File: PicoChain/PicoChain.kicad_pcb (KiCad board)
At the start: 2 copper layers, 14 parts, among them J1 RJ45, J2 RJ45, J3 Conn_01x02_Socket, J4 Conn_01x02_Socket, J5 Conn_01x20_Socket, J6 Conn_01x20_Socket, U1 PCA9615DP, U2 RASPBERRY_PI_PICO

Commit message: Updated to version 1.1
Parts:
- removed J3, J4: Conn_01x02_Socket, Connector_PinHeader_2.54mm:PinHeader_1x02_P2.54mm_Vertical
- removed R1, R3, R4, R6: 470, Resistor_SMD:R_0805_2012Metric
- removed R2, R5: 140, Resistor_SMD:R_0805_2012Metric
- added +12V: GND, Connector_PinHeader_2.54mm:PinHeader_1x02_P2.54mm_Vertical, F.Cu at (128.5, 112.6)
- added +5V: GND, Connector_PinHeader_2.54mm:PinHeader_1x02_P2.54mm_Vertical, F.Cu at (128.5, 96.1)
- added C1: 330nF, Capacitor_Tantalum_SMD:CP_EIA-3216-18_Kemet-A, F.Cu at (150.4, 82.6)
- added C2: 330nF, Capacitor_Tantalum_SMD:CP_EIA-3216-18_Kemet-A, F.Cu at (165.6, 82.9)
- added C3: 330nF, Capacitor_Tantalum_SMD:CP_EIA-3216-18_Kemet-A, F.Cu at (162.1, 82.9)
- added C4: 330nF, Capacitor_Tantalum_SMD:CP_EIA-3216-18_Kemet-A, F.Cu at (153.9, 82.6)
- added C5: 10uF, Capacitor_Tantalum_SMD:CP_EIA-3528-21_Kemet-B, F.Cu at (158.8, 108.8)
- added C6: 10uF, Capacitor_Tantalum_SMD:CP_EIA-3528-21_Kemet-B, F.Cu at (158.8, 104.0)
- added U3: LM78M05, Package_TO_SOT_SMD:TO-252-2, F.Cu at (163.3, 73.8)
- added U4: LM78M05, Package_TO_SOT_SMD:TO-252-2, F.Cu at (152.7, 73.7)
- added U5: LM1085-12, LM1085IS-12:TO254P1524X483-4N, F.Cu at (170.2, 105.0)
- U2: footprint MCU_RaspberryPi_and_Boards:RPi_Pico_SMD_TH -> RASPBERRY_PI_PICO:RASPBERRY_PI_PICO
- moved J6 93.2 mm to (182.0, 119.6), turned to -90 degrees
- moved J5 45.2 mm to (133.7, 91.7), turned to 90 degrees
- moved U2 38.1 mm to (159.1, 105.7), turned to -90 degrees
- moved J1 34.2 mm to (143.7, 83.4), turned to 180 degrees
- moved J2 29.5 mm to (181.8, 83.4), turned to 180 degrees
- moved U1 20.9 mm to (158.3, 85.2), turned to 90 degrees
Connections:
- J1 pad 1: Net-(U1-DSCLM) -> GND
- J1 pad 2: Net-(U1-DSCLP) -> +24V
- J1 pad 3: +5V -> Net-(U1-DSCLM)
- J1 pad 4: GND -> Net-(U1-DSCLP)
- J1 pad 5: /+5V(M) -> Net-(U1-DSDAP)
- J1 pad 6: +12V -> Net-(U1-DSDAM)
- J1 pad 7: Net-(U1-DSDAM) -> GND
- J1 pad 8: Net-(U1-DSDAP) -> +12V
- J2 pad 1: Net-(U1-DSCLM) -> GND
- J2 pad 2: Net-(U1-DSCLP) -> +24V
- J2 pad 3: +5V -> Net-(U1-DSCLM)
- J2 pad 4: GND -> Net-(U1-DSCLP)
- J2 pad 5: /+5V(M) -> Net-(U1-DSDAP)
- J2 pad 6: +12V -> Net-(U1-DSDAM)
- J2 pad 7: Net-(U1-DSDAM) -> GND
- J2 pad 8: Net-(U1-DSDAP) -> +12V
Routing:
- net +24V: track 0.00 -> 86.2 mm, vias 0 -> 1
- net +5V: track 0.00 -> 84.0 mm
- net +12V: track 0.00 -> 83.4 mm, vias 0 -> 1
- net Net-(U1-DSCLP): track 0.00 -> 50.7 mm, vias 0 -> 2
- net Net-(U1-DSDAM): track 0.00 -> 49.9 mm, vias 0 -> 2
- net /+5V(M): track 0.00 -> 45.6 mm, vias 0 -> 1
- net Net-(U1-DSDAP): track 0.00 -> 43.9 mm, vias 0 -> 2
- net Net-(U1-DSCLM): track 0.00 -> 43.2 mm, vias 0 -> 2
- net /+12V(R): track 0.00 -> 39.3 mm
- net Net-(J5-Pin_15): track 0.00 -> 27.9 mm, vias 0 -> 1
- net Net-(J5-Pin_14): track 0.00 -> 26.3 mm, vias 0 -> 1
- net Net-(J6-Pin_9): track 0.00 -> 5.08 mm
- net Net-(J6-Pin_8): track 0.00 -> 5.08 mm
- net Net-(J6-Pin_7): track 0.00 -> 5.08 mm
- net Net-(J6-Pin_6): track 0.00 -> 5.08 mm
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- added copper zone on B.Cu, net GND
- added copper zone on F.Cu, net GND
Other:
- board outline added: 60 x 54 mm
- board text added: "Jason Alexander"
- board text added: "PicoDaisy"
- board text added: "PicoDaisy (v1.1)"

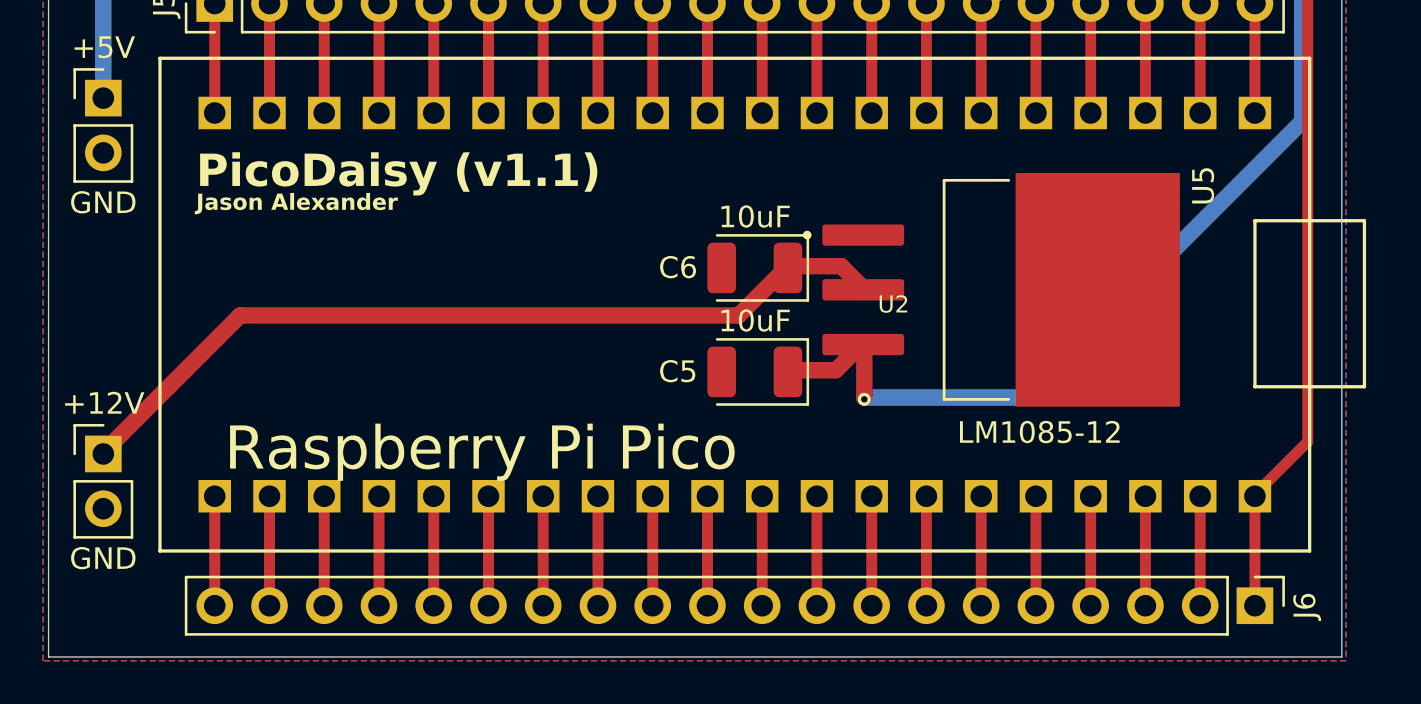
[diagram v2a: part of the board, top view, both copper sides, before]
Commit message: Added open source hardware logo to PCBs
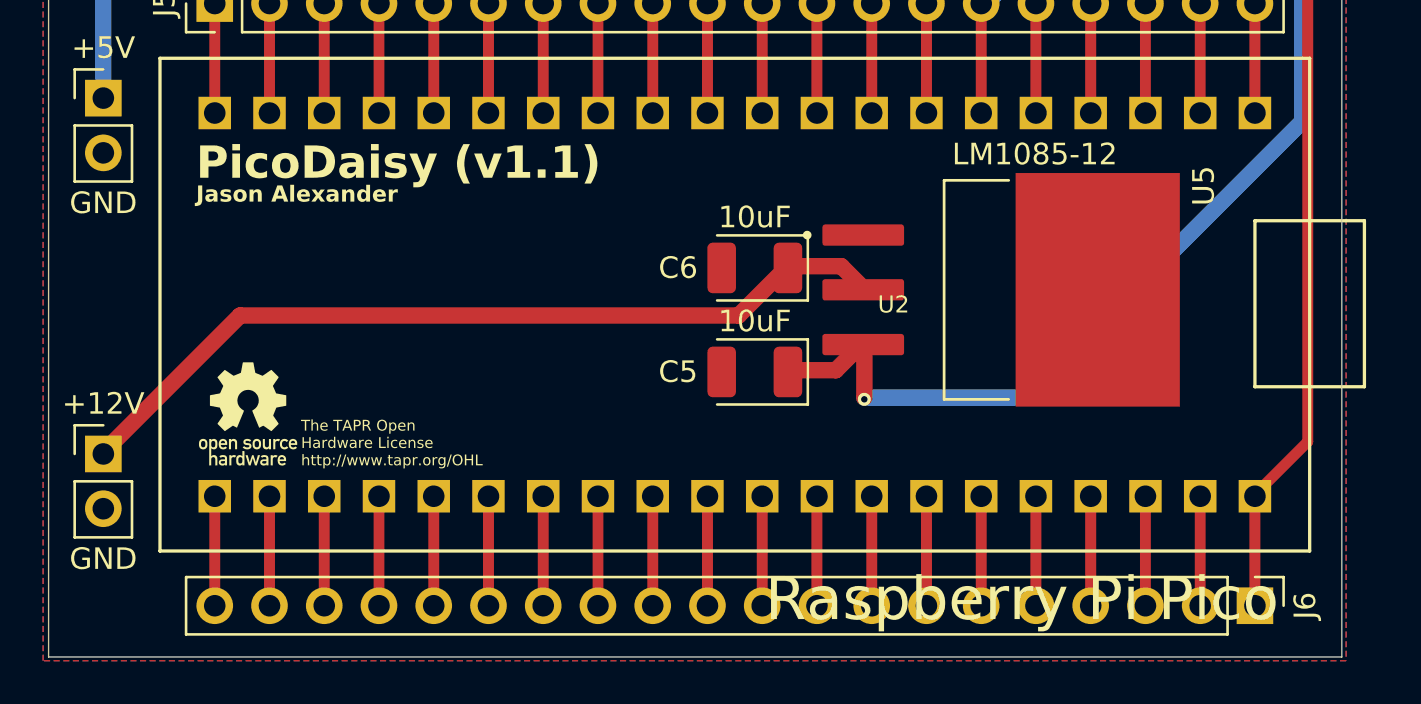
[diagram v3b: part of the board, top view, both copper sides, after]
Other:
- board text added: "The TAPR Open Hardware License http://www.tapr.org/OHL"

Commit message: Regenerated gerbers
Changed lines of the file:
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@@
 		)
 		(fp_text user "Raspberry Pi Pico"
-			(at 13.663056 -12.054914 0)
+			(at 0.0114 15.5994 0)
 			(layer "F.SilkS")
 			(effects
 				(font
-					(size 2 2)
+					(size 1.75 1.75)
 					(thickness 0.15)
 				)

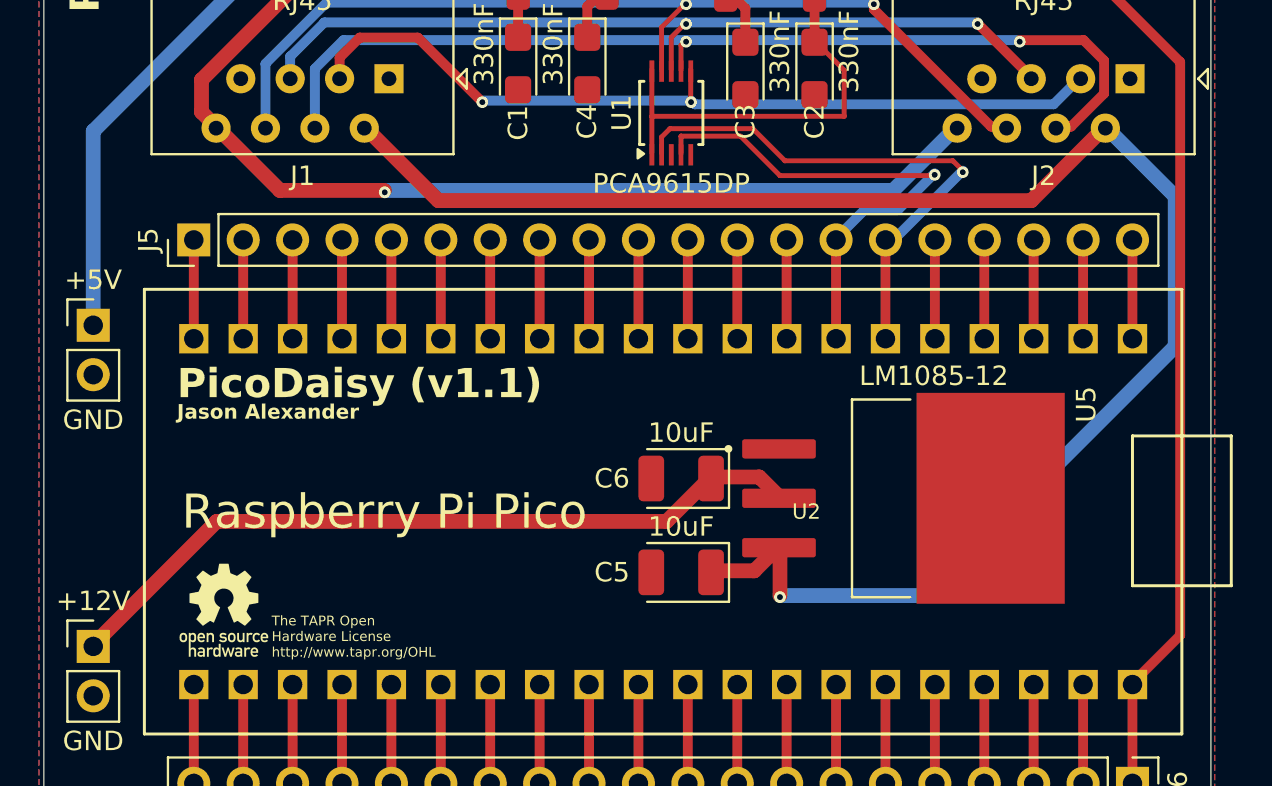
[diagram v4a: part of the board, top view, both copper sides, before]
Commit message: Made pass through power rails larger.
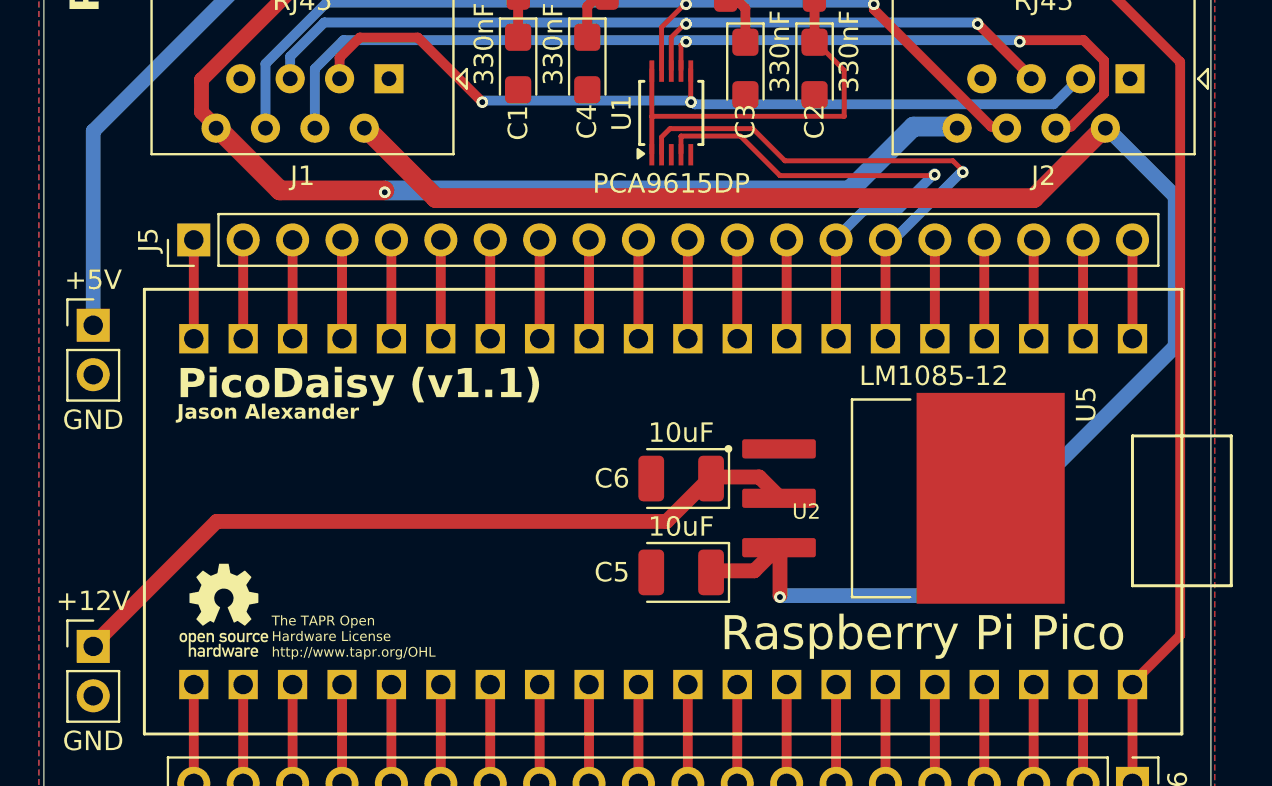
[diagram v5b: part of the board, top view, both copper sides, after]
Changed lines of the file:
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@@
 		)
 		(fp_text user "Raspberry Pi Pico"
-			(at 0.0114 15.5994 0)
+			(at 6.2598 -12.0866 0)
 			(layer "F.SilkS")
 			(effects
@@
 		(start 138.1365 89.138)
 		(end 143.51 89.138)
-		(width 0.762)
+		(width 1.016)
 		(layer "F.Cu")
 		(net 5)
@@
 		(start 134.8545 85.856)
 		(end 138.1365 89.138)
-		(width 0.762)
+		(width 1.016)
 		(layer "F.Cu")
 		(net 5)
@@
 	)
 	(segment
+		(start 167.4274 89.138)
+		(end 170.7094 85.856)
+		(width 1.016)
+		(layer "B.Cu")
+		(net 5)
+	)
+	(segment
 		(start 143.51 89.138)
 		(end 143.526 89.154)
@@
 	)
 	(segment
-		(start 169.6725 89.138)
-		(end 172.9545 85.856)
+		(start 143.526 89.154)
+		(end 143.542 89.138)
 		(width 0.762)
 		(layer "B.Cu")
@@
 	)
 	(segment
-		(start 143.542 89.138)
-		(end 169.6725 89.138)
-		(width 0.762)
+		(start 170.7094 85.856)
+		(end 172.9545 85.856)
+		(width 1.016)
 		(layer "B.Cu")
 		(net 5)
 	)
 	(segment
-		(start 143.526 89.154)
-		(end 143.542 89.138)
-		(width 0.762)
+		(start 143.542 89.138)
+		(end 167.4274 89.138)
+		(width 1.016)
 		(layer "B.Cu")
 		(net 5)
@@
 	)
 	(segment
-		(start 176.7685 89.662)
+		(start 176.8955 89.535)
 		(end 180.5745 85.856)
-		(width 0.762)
+		(width 1.016)
 		(layer "F.Cu")
 		(net 48)
 	)
 	(segment
-		(start 142.4745 85.856)
-		(end 146.2805 89.662)
+		(start 163.846 107.476)
+		(end 163.796 107.426)
 		(width 0.762)
 		(layer "F.Cu")
@@
 	)
 	(segment
-		(start 163.846 107.476)
+		(start 162.526 108.696)
 		(end 163.796 107.426)
 		(width 0.762)
@@
 	)
 	(segment
-		(start 146.2805 89.662)
-		(end 176.7685 89.662)
-		(width 0.762)
+		(start 146.1535 89.535)
+		(end 176.8955 89.535)
+		(width 1.016)
 		(layer "F.Cu")
 		(net 48)
 	)
 	(segment
-		(start 162.526 108.696)
-		(end 163.796 107.426)
-		(width 0.762)
+		(start 142.4745 85.856)
+		(end 146.1535 89.535)
+		(width 1.016)
 		(layer "F.Cu")
 		(net 48)

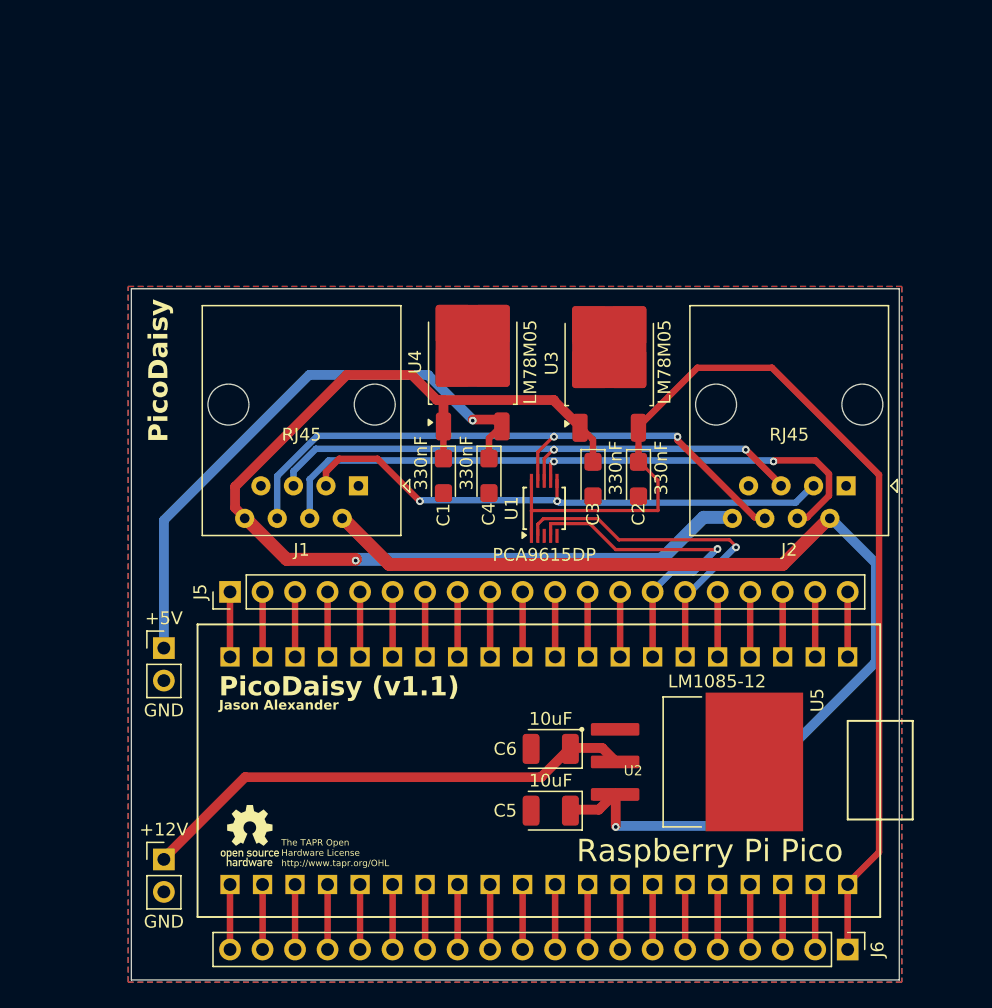
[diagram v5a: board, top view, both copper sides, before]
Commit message: Updated PicoChainZero base board.
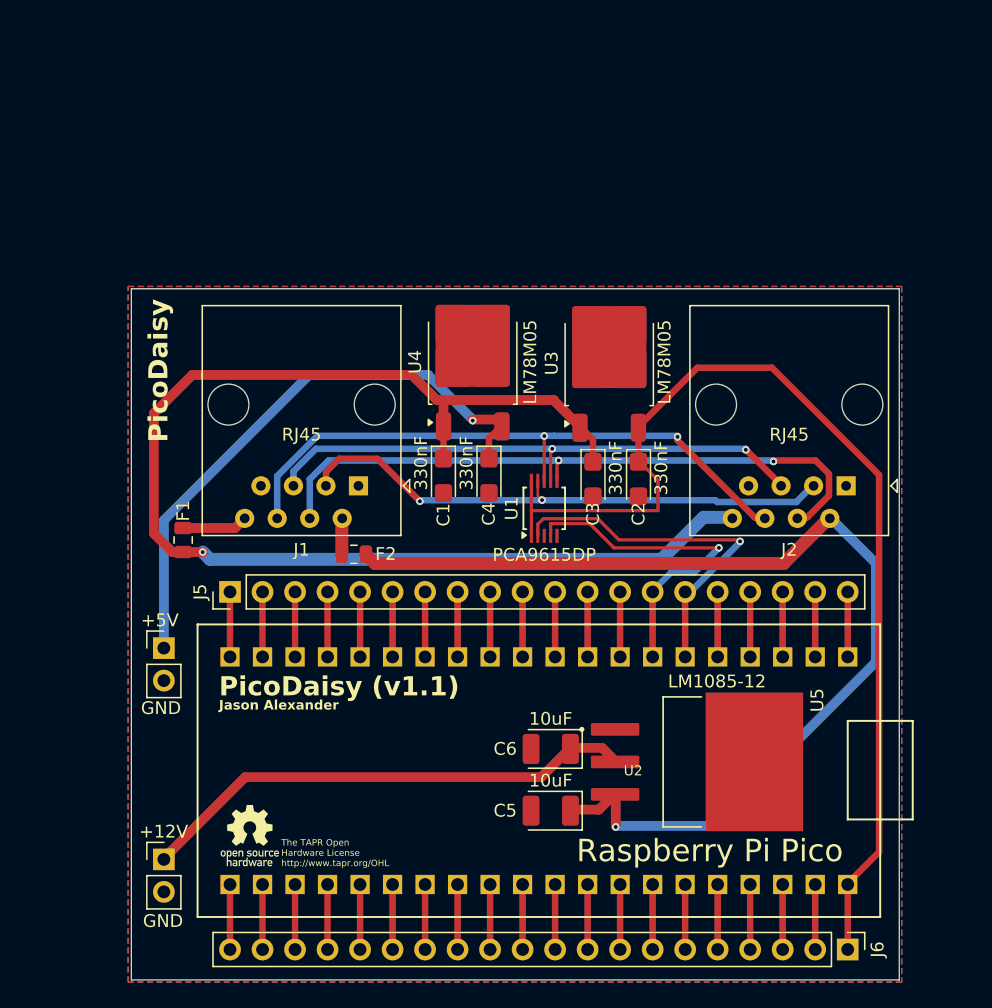
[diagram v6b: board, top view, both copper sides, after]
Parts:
- added F1: Fuse, Fuse:Fuse_0805_2012Metric, F.Cu at (130.0, 87.6)
- added F2: Fuse, Fuse:Fuse_0805_2012Metric, F.Cu at (143.4, 88.7)
- J3: renamed from +12V; value GND -> Conn_01x02_Socket
- J4: renamed from +5V; value GND -> Conn_01x02_Socket
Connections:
- J1 pad 2: +24V -> Net-(F2-Pad1)
- J1 pad 3: Net-(U1-DSCLM) -> Net-(U1-DSDAM)
- J1 pad 4: Net-(U1-DSCLP) -> Net-(U1-DSCLM)
- J1 pad 5: Net-(U1-DSDAP) -> Net-(U1-DSCLP)
- J1 pad 6: Net-(U1-DSDAM) -> Net-(U1-DSDAP)
- J1 pad 8: +12V -> Net-(F1-Pad1)
- J2 pad 3: Net-(U1-DSCLM) -> Net-(U1-DSDAM)
- J2 pad 4: Net-(U1-DSCLP) -> Net-(U1-DSCLM)
- J2 pad 5: Net-(U1-DSDAP) -> Net-(U1-DSCLP)
- J2 pad 6: Net-(U1-DSDAM) -> Net-(U1-DSDAP)
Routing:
- net +12V: track 83.4 -> 100.6 mm
- net Net-(U1-DSCLM): track 43.2 -> 50.7 mm
- net Net-(U1-DSCLP): track 50.7 -> 43.7 mm
- net Net-(U1-DSDAM): track 49.9 -> 43.2 mm
- net Net-(U1-DSDAP): track 43.9 -> 49.4 mm
- net Net-(F1-Pad1): track 0.00 -> 5.12 mm
- net +24V: track 86.1 -> 83.0 mm
- net Net-(F2-Pad1): track 0.00 -> 2.82 mm
- net Net-(J5-Pin_15): track 27.9 -> 28.6 mm
- added copper zone on In1.Cu, net GND
- added copper zone on In2.Cu, net GND
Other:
- copper layers 2 -> 4
- board text added: "+12V"
- board text added: "+5V"
- board text added: "GND"
